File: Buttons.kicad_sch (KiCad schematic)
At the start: 40 parts, among them SW10 MX_SW_solder, SW11 MX_SW_HS, SW12 MX_SW_solder, SW13 MX_SW_HS, SW14 MX_SW_HS, SW15 MX_SW_solder, SW16 MX_SW_HS, SW17 MX_SW_solder, SW18 MX_SW_HS, SW19 MX_SW_solder, SW2 MX_SW_HS, SW20 MX_SW_solder, SW21 MX_SW_HS, SW22 MX_SW_solder, SW23 MX_SW_HS, SW24 MX_SW_solder, SW25 MX_SW_HS, SW26 MX_SW_solder, SW27 MX_SW_HS, SW28 MX_SW_solder, SW29 MX_SW_HS, SW3 MX_SW_solder, SW30 MX_SW_solder, SW31 MX_SW_HS, SW32 MX_SW_HS, SW33 MX_SW_solder, SW34 MX_SW_solder, SW35 MX_SW_HS, SW36 MX_SW_HS, SW37 MX_SW_solder, SW38 MX_SW_solder, SW39 MX_SW_HS, SW4 MX_SW_HS, SW40 MX_SW_solder, SW41 MX_SW_HS, SW5 MX_SW_solder, SW6 MX_SW_HS, SW7 MX_SW_solder, SW8 MX_SW_HS, SW9 MX_SW_solder

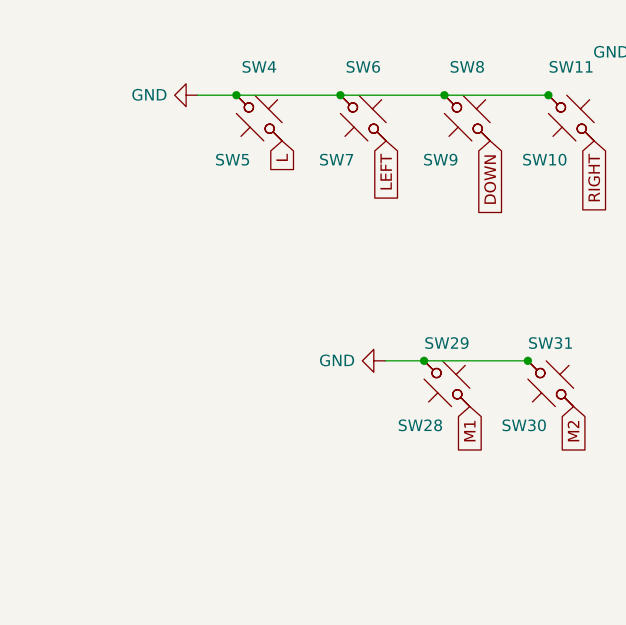
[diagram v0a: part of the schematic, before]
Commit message: Added optional buttons
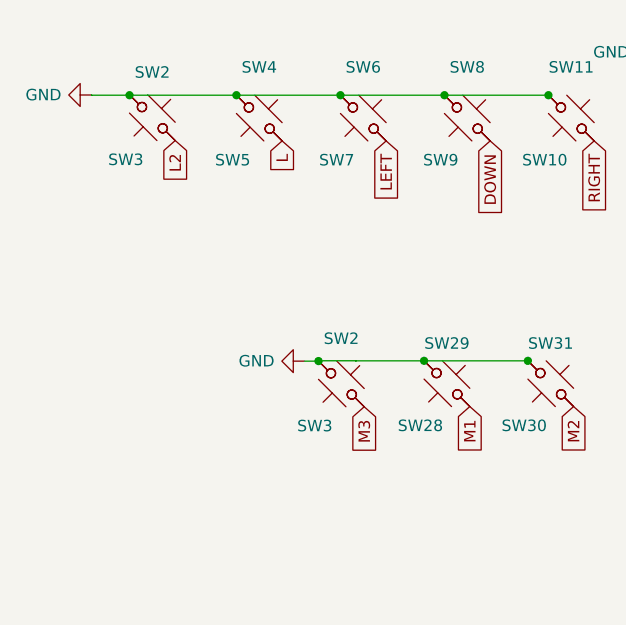
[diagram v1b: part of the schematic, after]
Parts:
- added SW2 (x2): MX_SW_HS, marbastlib-mx:SW_MX_HS_1u, symbol marbastlib-mx:MX_SW_HS
- added SW3 (x2): MX_SW_solder, marbastlib-mx:SW_MX_1u, symbol marbastlib-mx:MX_SW_solder
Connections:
- net GND: now also SW2.1, SW2.1, SW3.2, SW3.2
- new net L2: SW2.2, SW3.1
- new net M3: SW2.2, SW3.1
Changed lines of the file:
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@@
   (junction (at 87.503 29.718) (diameter 0) (color 0 0 0 0)
   )
+  (junction (at 61.9534 59.2582) (diameter 0) (color 0 0 0 0)
+  )
   (junction (at 64.389 29.718) (diameter 0) (color 0 0 0 0)
   )
@@
   (junction (at 99.822 24.9428) (diameter 0) (color 0 0 0 0)
   )
+  (junction (at 40.953 29.718) (diameter 0) (color 0 0 0 0)
+  )
   (junction (at 145.161 48.4632) (diameter 0) (color 0 0 0 0)
   )
@@
   (junction (at 113.03 66.4464) (diameter 0) (color 0 0 0 0)
   )
+  (wire (pts (xy 36.7426 29.718) (xy 36.7426 29.6944))
+    (stroke (width 0) (type default))
+  )
   (wire (pts (xy 117.7544 48.4632) (xy 122.047 48.4632))
     (stroke (width 0) (type default))
@@
     (stroke (width 0) (type default))
   )
-  (wire (pts (xy 48.514 29.718) (xy 52.832 29.718))
-    (stroke (width 0) (type default))
-  )
   (wire (pts (xy 116.8908 31.6484) (xy 121.2088 31.6484))
     (stroke (width 0) (type default))
@@
     (stroke (width 0) (type default))
   )
+  (wire (pts (xy 40.953 29.718) (xy 40.953 29.6757))
+    (stroke (width 0) (type default))
+  )
   (wire (pts (xy 73.6854 59.2328) (xy 85.217 59.2328))
     (stroke (width 0) (type default))
@@
     (stroke (width 0) (type default))
   )
-  (wire (pts (xy 69.3674 59.2328) (xy 73.6854 59.2328))
+  (wire (pts (xy 61.9534 59.2582) (xy 61.9534 59.2237))
     (stroke (width 0) (type default))
   )
@@
     (stroke (width 0) (type default))
   )
+  (wire (pts (xy 66.1027 59.2328) (xy 73.6854 59.2328))
+    (stroke (width 0) (type default))
+  )
+  (wire (pts (xy 60.4203 59.2673) (xy 61.9534 59.2673))
+    (stroke (width 0) (type default))
+  )
   (wire (pts (xy 122.047 48.4632) (xy 133.604 48.4632))
     (stroke (width 0) (type default))
   )
+  (wire (pts (xy 36.7426 29.718) (xy 40.953 29.718))
+    (stroke (width 0) (type default))
+  )
+  (wire (pts (xy 66.1027 59.2237) (xy 66.1027 59.2328))
+    (stroke (width 0) (type default))
+  )
   (wire (pts (xy 113.03 66.4464) (xy 124.5616 66.4464))
     (stroke (width 0) (type default))
   )
+  (wire (pts (xy 61.9534 59.2237) (xy 66.1027 59.2237))
+    (stroke (width 0) (type default))
+  )
   (wire (pts (xy 64.389 29.718) (xy 75.946 29.718))
     (stroke (width 0) (type default))
   )
+  (wire (pts (xy 61.9534 59.2673) (xy 61.9534 59.2582))
+    (stroke (width 0) (type default))
+  )
   (wire (pts (xy 121.2088 31.6484) (xy 132.7404 31.6484))
     (stroke (width 0) (type default))
@@
     (stroke (width 0) (type default))
   )
+  (wire (pts (xy 40.953 29.718) (xy 52.832 29.718))
+    (stroke (width 0) (type default))
+  )
   (global_label "DOWN" (shape input) (at 81.026 34.798 270) (fields_autoplaced)
     (effects (font (size 1.27 1.27)) (justify right))
@@
     )
   )
+  (global_label "M3" (shape input) (at 67.0334 64.3382 270) (fields_autoplaced)
+    (effects (font (size 1.27 1.27)) (justify right))
+    (property "Intersheetrefs" "${INTERSHEET_REFS}" (at 67.0334 69.9049 90)
+      (effects (font (size 1.27 1.27)) (justify right) hide)
+    )
+  )
   (global_label "C_RT" (shape input) (at 133.0198 89.0778 270) (fields_autoplaced)
     (effects (font (size 1.27 1.27)) (justify right))
@@
     )
   )
+  (global_label "L2" (shape input) (at 46.033 34.7557 270) (fields_autoplaced)
+    (effects (font (size 1.27 1.27)) (justify right))
+    (property "Intersheetrefs" "${INTERSHEET_REFS}" (at 46.033 39.8991 90)
+      (effects (font (size 1.27 1.27)) (justify right) hide)
+    )
+  )
   (global_label "START" (shape input) (at 104.902 30.0228 270) (fields_autoplaced)
     (effects (font (size 1.27 1.27)) (justify right))
@@
         (path "/0ee7bd02-e26d-4978-ae8c-675a718c78c0/ab81b747-dd98-4419-bfbb-bd9e2c783c49"
           (reference "SW38") (unit 1)
+        )
+      )
+    )
+  )
+  (symbol (lib_id "marbastlib-mx:MX_SW_solder") (at 43.493 32.2157 180) (unit 1)
+    (in_bom yes) (on_board yes) (dnp no)
+    (property "Reference" "SW3" (at 40.5466 36.8893 0)
+      (effects (font (size 1.27 1.27)))
+    )
+    (property "Value" "MX_SW_solder" (at 43.493 37.8037 0)
+      (effects (font (size 1.27 1.27)) hide)
+    )
+    (property "Footprint" "marbastlib-mx:SW_MX_1u" (at 43.493 32.2157 0)
+      (effects (font (size 1.27 1.27)) hide)
+    )
+    (property "Datasheet" "~" (at 43.493 32.2157 0)
+      (effects (font (size 1.27 1.27)) hide)
+    )
+    (pin "1")
+    (pin "2")
+    (instances
+      (project "OpenRectangle"
+        (path "/0ee7bd02-e26d-4978-ae8c-675a718c78c0"
+          (reference "SW3") (unit 1)
+        )
+        (path "/0ee7bd02-e26d-4978-ae8c-675a718c78c0/ab81b747-dd98-4419-bfbb-bd9e2c783c49"
+          (reference "SW42") (unit 1)
+        )
+      )
+    )
+  )
+  (symbol (lib_id "marbastlib-mx:MX_SW_HS") (at 43.493 32.2157 0) (unit 1)
+    (in_bom yes) (on_board yes) (dnp no) (fields_autoplaced)
+    (property "Reference" "SW2" (at 43.493 27.1865 0)
+      (effects (font (size 1.27 1.27)))
+    )
+    (property "Value" "MX_SW_HS" (at 43.493 27.5167 0)
+      (effects (font (size 1.27 1.27)) hide)
+    )
+    (property "Footprint" "marbastlib-mx:SW_MX_HS_1u" (at 43.493 32.2157 0)
+      (effects (font (size 1.27 1.27)) hide)
+    )
+    (property "Datasheet" "~" (at 43.493 32.2157 0)
+      (effects (font (size 1.27 1.27)) hide)
+    )
+    (pin "1")
+    (pin "2")
+    (instances
+      (project "OpenRectangle"
+        (path "/0ee7bd02-e26d-4978-ae8c-675a718c78c0"
+          (reference "SW2") (unit 1)
+        )
+        (path "/0ee7bd02-e26d-4978-ae8c-675a718c78c0/ab81b747-dd98-4419-bfbb-bd9e2c783c49"
+          (reference "SW43") (unit 1)
+        )
+      )
+    )
+  )
+  (symbol (lib_id "marbastlib-mx:MX_SW_HS") (at 64.4934 61.7982 0) (unit 1)
+    (in_bom yes) (on_board yes) (dnp no) (fields_autoplaced)
+    (property "Reference" "SW2" (at 64.4934 56.769 0)
+      (effects (font (size 1.27 1.27)))
+    )
+    (property "Value" "MX_SW_HS" (at 64.4934 57.0992 0)
+      (effects (font (size 1.27 1.27)) hide)
+    )
+    (property "Footprint" "marbastlib-mx:SW_MX_HS_1u" (at 64.4934 61.7982 0)
+      (effects (font (size 1.27 1.27)) hide)
+    )
+    (property "Datasheet" "~" (at 64.4934 61.7982 0)
+      (effects (font (size 1.27 1.27)) hide)
+    )
+    (pin "1")
+    (pin "2")
+    (instances
+      (project "OpenRectangle"
+        (path "/0ee7bd02-e26d-4978-ae8c-675a718c78c0"
+          (reference "SW2") (unit 1)
+        )
+        (path "/0ee7bd02-e26d-4978-ae8c-675a718c78c0/ab81b747-dd98-4419-bfbb-bd9e2c783c49"
+          (reference "SW44") (unit 1)
         )
       )
@@
     )
   )
-  (symbol (lib_id "power:GND") (at 69.3674 59.2328 270) (unit 1)
-    (in_bom yes) (on_board yes) (dnp no) (fields_autoplaced)
-    (property "Reference" "#PWR036" (at 63.0174 59.2328 0)
-      (effects (font (size 1.27 1.27)) hide)
-    )
-    (property "Value" "GND" (at 66.0146 59.2327 90)
+  (symbol (lib_id "power:GND") (at 60.4203 59.2673 270) (unit 1)
+    (in_bom yes) (on_board yes) (dnp no) (fields_autoplaced)
+    (property "Reference" "#PWR036" (at 54.0703 59.2673 0)
+      (effects (font (size 1.27 1.27)) hide)
+    )
+    (property "Value" "GND" (at 57.0675 59.2672 90)
       (effects (font (size 1.27 1.27)) (justify right))
     )
-    (property "Footprint" "" (at 69.3674 59.2328 0)
-      (effects (font (size 1.27 1.27)) hide)
-    )
-    (property "Datasheet" "" (at 69.3674 59.2328 0)
+    (property "Footprint" "" (at 60.4203 59.2673 0)
+      (effects (font (size 1.27 1.27)) hide)
+    )
+    (property "Datasheet" "" (at 60.4203 59.2673 0)
       (effects (font (size 1.27 1.27)) hide)
     )
@@
     )
   )
+  (symbol (lib_id "marbastlib-mx:MX_SW_solder") (at 64.4934 61.7982 180) (unit 1)
+    (in_bom yes) (on_board yes) (dnp no)
+    (property "Reference" "SW3" (at 61.547 66.4718 0)
+      (effects (font (size 1.27 1.27)))
+    )
+    (property "Value" "MX_SW_solder" (at 64.4934 67.3862 0)
+      (effects (font (size 1.27 1.27)) hide)
+    )
+    (property "Footprint" "marbastlib-mx:SW_MX_1u" (at 64.4934 61.7982 0)
+      (effects (font (size 1.27 1.27)) hide)
+    )
+    (property "Datasheet" "~" (at 64.4934 61.7982 0)
+      (effects (font (size 1.27 1.27)) hide)
+    )
+    (pin "1")
+    (pin "2")
+    (instances
+      (project "OpenRectangle"
+        (path "/0ee7bd02-e26d-4978-ae8c-675a718c78c0"
+          (reference "SW3") (unit 1)
+        )
+        (path "/0ee7bd02-e26d-4978-ae8c-675a718c78c0/ab81b747-dd98-4419-bfbb-bd9e2c783c49"
+          (reference "SW45") (unit 1)
+        )
+      )
+    )
+  )
   (symbol (lib_id "marbastlib-mx:MX_SW_HS") (at 159.258 51.0032 0) (unit 1)
     (in_bom yes) (on_board yes) (dnp no) (fields_autoplaced)
@@
     )
   )
-  (symbol (lib_id "power:GND") (at 48.514 29.718 270) (unit 1)
-    (in_bom yes) (on_board yes) (dnp no) (fields_autoplaced)
-    (property "Reference" "#PWR033" (at 42.164 29.718 0)
-      (effects (font (size 1.27 1.27)) hide)
-    )
-    (property "Value" "GND" (at 45.1612 29.7179 90)
+  (symbol (lib_id "power:GND") (at 36.7426 29.6944 270) (unit 1)
+    (in_bom yes) (on_board yes) (dnp no) (fields_autoplaced)
+    (property "Reference" "#PWR033" (at 30.3926 29.6944 0)
+      (effects (font (size 1.27 1.27)) hide)
+    )
+    (property "Value" "GND" (at 33.3898 29.6943 90)
       (effects (font (size 1.27 1.27)) (justify right))
     )
-    (property "Footprint" "" (at 48.514 29.718 0)
-      (effects (font (size 1.27 1.27)) hide)
-    )
-    (property "Datasheet" "" (at 48.514 29.718 0)
-      (effects (font (size 1.27 1.27)) hide)
-    )
+    (property "Footprint" "" (at 36.7426 29.6944 0)
+      (effects (font (size 1.27 1.27)) hide)
+    )
+    (property "Datasheet" "" (at 36.7426 29.6944 0)
+      (effects (font (size 1.27 1.27)) hide)
+    )
